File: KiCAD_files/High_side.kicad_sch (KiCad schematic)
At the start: 26 parts, among them U601 AMC1311DWV

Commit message: WIP
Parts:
- removed TP? (x4): TestPoint, Footprints:TestPoint_THTPad_D1.5mm_Drill0.7mm, symbol Connector:TestPoint
- added TP202 (x4): TestPoint, Footprints:TestPoint_THTPad_D1.5mm_Drill0.7mm, symbol Connector:TestPoint
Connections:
- net DGND: now also TP202.1, TP202.1
- net I_{IHigh_sense_DGND}: now also TP202.1
- net V_{IHighOutFused_PGND}: now also U?.1 (IP+), U?.2 (IP+); no longer U?.3 (IP-), U?.4 (IP-)
- net V_{IHigh_PGND}: now also U?.3 (IP-), U?.4 (IP-); no longer U?.1 (IP+), U?.2 (IP+)
- net V_{IHigh_sense_DGND}: now also TP202.1
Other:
- moved on the sheet: U?

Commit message: big clean in libraries (imported components in symbol), PCB WIP
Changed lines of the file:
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@@
     )
     (property "Value" "OPA316" (at 128.27 190.5 0)
-      (effects (font (size 1.27 1.27)) (justify left))
+      (effects (font (size 1.27 1.27)) (justify left) hide)
     )
     (property "Footprint" "Package_TO_SOT_SMD:SOT-353_SC-70-5_Handsoldering" (at 130.81 199.39 0)
@@
     )
     (property "manf#" "OPA316IDCKT" (at 125.73 194.31 0)
-      (effects (font (size 1.27 1.27)) hide)
+      (effects (font (size 1.27 1.27)))
     )
     (pin "1")

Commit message: Ready for design review
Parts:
- removed C? (x2): 100nF, Footprints:C_0805_2012Metric, symbol Device:C_Small
- added C? (x2): 100nF, Capacitor_SMD:C_1206_3216Metric, symbol Device:C_Small
- C?: footprint Footprints:C_0805_2012Metric -> Capacitor_SMD:C_1206_3216Metric; Functional Block (none) -> Measurement; Metal content (none) -> BaTiO3; Package 0805 -> 1206; Subfunction (none) -> VIHigh measure; manf# C0805C104K5RACTU -> C1206C104K5RAC7867
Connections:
- net +5V_DGND: now also C?.2
- net +5V_PGND: now also C?.2
- net DGND: now also C?.1
- net PGND: now also C?.1
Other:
- moved on the sheet: C?
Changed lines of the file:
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@@
     (stroke (width 0.35) (type default))
   )
-  (wire (pts (xy 88.9 170.18) (xy 88.9 171.45))
+  (wire (pts (xy 88.9 170.18) (xy 88.9 172.72))
     (stroke (width 0) (type default))
   )
@@
     (stroke (width 0) (type default))
   )
-  (wire (pts (xy 88.9 176.53) (xy 88.9 180.34))
+  (wire (pts (xy 88.9 177.8) (xy 88.9 180.34))
     (stroke (width 0) (type default))
   )
@@
     )
   )
-  (symbol (lib_id "Device:C_Small") (at 88.9 173.99 0) (mirror x) (unit 1)
-    (in_bom yes) (on_board yes) (dnp no)
-    (property "Reference" "C?" (at 91.44 172.72 0)
-      (effects (font (size 1.27 1.27)) (justify left))
-    )
-    (property "Value" "100nF" (at 90.17 176.53 0)
-      (effects (font (size 1.27 1.27)) (justify left))
-    )
-    (property "Footprint" "Footprints:C_0805_2012Metric" (at 88.9 173.99 0)
-      (effects (font (size 1.27 1.27)) hide)
-    )
-    (property "Datasheet" "~" (at 88.9 173.99 0)
-      (effects (font (size 1.27 1.27)) hide)
-    )
-    (property "manf#" "C0805C104K5RACTU" (at 88.9 173.99 0)
-      (effects (font (size 1.27 1.27)) hide)
-    )
-    (property "DNP" "x" (at 88.9 173.99 0)
-      (effects (font (size 1.27 1.27)) hide)
-    )
-    (property "Voltage" "50V" (at 87.63 170.18 90)
-      (effects (font (size 1.27 1.27)) hide)
-    )
-    (property "Package" "0805" (at 91.44 170.18 90)
+  (symbol (lib_id "Device:C_Small") (at 88.9 175.26 0) (mirror x) (unit 1)
+    (in_bom yes) (on_board yes) (dnp no)
+    (property "Reference" "C?" (at 91.44 173.99 0)
+      (effects (font (size 1.27 1.27)) (justify left))
+    )
+    (property "Value" "100nF" (at 91.44 176.53 0)
+      (effects (font (size 1.27 1.27)) (justify left))
+    )
+    (property "Footprint" "Capacitor_SMD:C_1206_3216Metric" (at 88.9 175.26 0)
+      (effects (font (size 1.27 1.27)) hide)
+    )
+    (property "Datasheet" "~" (at 88.9 175.26 0)
+      (effects (font (size 1.27 1.27)) hide)
+    )
+    (property "manf#" "C1206C104K5RAC7867" (at 88.9 175.26 0)
+      (effects (font (size 1.27 1.27)) hide)
+    )
+    (property "DNP" "x" (at 88.9 175.26 0)
+      (effects (font (size 1.27 1.27)) hide)
+    )
+    (property "Voltage" "50V" (at 87.63 171.45 90)
+      (effects (font (size 1.27 1.27)) hide)
+    )
+    (property "Package" "1206" (at 93.98 179.07 0)
+      (effects (font (size 1.27 1.27)))
+    )
+    (property "Functional Block" "Measurement" (at 88.9 175.26 0)
+      (effects (font (size 1.27 1.27)) hide)
+    )
+    (property "Metal content" "BaTiO3" (at 88.9 175.26 0)
+      (effects (font (size 1.27 1.27)) hide)
+    )
+    (property "Subfunction" "VIHigh measure" (at 88.9 175.26 0)
       (effects (font (size 1.27 1.27)) hide)
     )
@@
         (path "/8d0c1d66-35ef-4a53-a28f-436a11b54f42/e045b567-5361-4b1d-a1af-a53fa67ecaba"
           (reference "R604") (unit 1)
-        )
-      )
-    )
-  )
-  (symbol (lib_id "Device:C_Small") (at 113.03 67.31 0) (mirror x) (unit 1)
-    (in_bom yes) (on_board yes) (dnp no)
-    (property "Reference" "C?" (at 115.57 66.04 0)
-      (effects (font (size 1.27 1.27)) (justify left))
-    )
-    (property "Value" "100nF" (at 114.3 69.85 0)
-      (effects (font (size 1.27 1.27)) (justify left))
-    )
-    (property "Footprint" "Footprints:C_0805_2012Metric" (at 113.03 67.31 0)
-      (effects (font (size 1.27 1.27)) hide)
-    )
-    (property "Datasheet" "~" (at 113.03 67.31 0)
-      (effects (font (size 1.27 1.27)) hide)
-    )
-    (property "manf#" "C0805C104K5RACTU" (at 113.03 67.31 0)
-      (effects (font (size 1.27 1.27)) hide)
-    )
-    (property "DNP" "x" (at 113.03 67.31 0)
-      (effects (font (size 1.27 1.27)) hide)
-    )
-    (property "Voltage" "50V" (at 111.76 63.5 90)
-      (effects (font (size 1.27 1.27)) hide)
-    )
-    (property "Package" "0805" (at 115.57 63.5 90)
-      (effects (font (size 1.27 1.27)) hide)
-    )
-    (pin "1")
-    (pin "2")
-    (instances
-      (project "InverterLeg"
-        (path "/22b63e0d-f11c-46a0-b2d0-b08207a579ff"
-          (reference "C?") (unit 1)
-        )
-      )
-      (project "Power"
-        (path "/8d0c1d66-35ef-4a53-a28f-436a11b54f42/122c01f4-f23e-4db0-9503-7261d96dc78b"
-          (reference "C?") (unit 1)
-        )
-        (path "/8d0c1d66-35ef-4a53-a28f-436a11b54f42/e045b567-5361-4b1d-a1af-a53fa67ecaba"
-          (reference "C604") (unit 1)
         )
       )
@@
     )
   )
-  (symbol (lib_id "Device:C_Small") (at 50.8 175.26 0) (mirror y) (unit 1)
-    (in_bom yes) (on_board yes) (dnp no)
-    (property "Reference" "C?" (at 48.26 176.53 0)
-      (effects (font (size 1.27 1.27)) (justify left))
-    )
-    (property "Value" "100nF" (at 49.53 172.72 0)
-      (effects (font (size 1.27 1.27)) (justify left))
-    )
-    (property "Footprint" "Footprints:C_0805_2012Metric" (at 50.8 175.26 0)
-      (effects (font (size 1.27 1.27)) hide)
-    )
-    (property "Datasheet" "~" (at 50.8 175.26 0)
-      (effects (font (size 1.27 1.27)) hide)
-    )
-    (property "manf#" "C0805C104K5RACTU" (at 50.8 175.26 0)
-      (effects (font (size 1.27 1.27)) hide)
-    )
-    (property "DNP" "x" (at 50.8 175.26 0)
-      (effects (font (size 1.27 1.27)) hide)
-    )
-    (property "Voltage" "50V" (at 52.07 179.07 90)
-      (effects (font (size 1.27 1.27)) hide)
-    )
-    (property "Package" "0805" (at 48.26 179.07 90)
+  (symbol (lib_id "Device:C_Small") (at 113.03 67.31 0) (mirror x) (unit 1)
+    (in_bom yes) (on_board yes) (dnp no)
+    (property "Reference" "C?" (at 115.57 66.04 0)
+      (effects (font (size 1.27 1.27)) (justify left))
+    )
+    (property "Value" "100nF" (at 115.57 68.58 0)
+      (effects (font (size 1.27 1.27)) (justify left))
+    )
+    (property "Footprint" "Capacitor_SMD:C_1206_3216Metric" (at 113.03 67.31 0)
+      (effects (font (size 1.27 1.27)) hide)
+    )
+    (property "Datasheet" "~" (at 113.03 67.31 0)
+      (effects (font (size 1.27 1.27)) hide)
+    )
+    (property "manf#" "C1206C104K5RAC7867" (at 113.03 67.31 0)
+      (effects (font (size 1.27 1.27)) hide)
+    )
+    (property "DNP" "x" (at 113.03 67.31 0)
+      (effects (font (size 1.27 1.27)) hide)
+    )
+    (property "Voltage" "50V" (at 111.76 63.5 90)
+      (effects (font (size 1.27 1.27)) hide)
+    )
+    (property "Package" "1206" (at 118.11 71.12 0)
+      (effects (font (size 1.27 1.27)))
+    )
+    (property "Functional Block" "Measurement" (at 113.03 67.31 0)
+      (effects (font (size 1.27 1.27)) hide)
+    )
+    (property "Metal content" "BaTiO3" (at 113.03 67.31 0)
+      (effects (font (size 1.27 1.27)) hide)
+    )
+    (property "Subfunction" "VIHigh measure" (at 113.03 67.31 0)
       (effects (font (size 1.27 1.27)) hide)
     )
@@
         )
         (path "/8d0c1d66-35ef-4a53-a28f-436a11b54f42/e045b567-5361-4b1d-a1af-a53fa67ecaba"
-          (reference "C601") (unit 1)
+          (reference "C604") (unit 1)
         )
       )
@@
         )
       )
+    )
+  )
+  (symbol (lib_id "Device:C_Small") (at 50.8 175.26 180) (unit 1)
+    (in_bom yes) (on_board yes) (dnp no)
+    (property "Reference" "C?" (at 48.26 173.99 0)
+      (effects (font (size 1.27 1.27)) (justify left))
+    )
+    (property "Value" "100nF" (at 48.26 176.53 0)
+      (effects (font (size 1.27 1.27)) (justify left))
+    )
+    (property "Footprint" "Capacitor_SMD:C_1206_3216Metric" (at 50.8 175.26 0)
+      (effects (font (size 1.27 1.27)) hide)
+    )
+    (property "Datasheet" "~" (at 50.8 175.26 0)
+      (effects (font (size 1.27 1.27)) hide)
+    )
+    (property "manf#" "C1206C104K5RAC7867" (at 50.8 175.26 0)
+      (effects (font (size 1.27 1.27)) hide)
+    )
+    (property "DNP" "x" (at 50.8 175.26 0)
+      (effects (font (size 1.27 1.27)) hide)
+    )
+    (property "Voltage" "50V" (at 52.07 171.45 90)
+      (effects (font (size 1.27 1.27)) hide)
+    )
+    (property "Package" "1206" (at 45.72 179.07 0)
+      (effects (font (size 1.27 1.27)))
+    )
+    (property "Functional Block" "Measurement" (at 50.8 175.26 0)
+      (effects (font (size 1.27 1.27)) hide)
+    )
+    (property "Metal content" "BaTiO3" (at 50.8 175.26 0)
+      (effects (font (size 1.27 1.27)) hide)
+    )
+    (property "Subfunction" "VIHigh measure" (at 50.8 175.26 0)
+      (effects (font (size 1.27 1.27)) hide)
+    )
+    (pin "1")
+    (pin "2")
+    (instances
+      (project "InverterLeg"
+        (path "/22b63e0d-f11c-46a0-b2d0-b08207a579ff"
+          (reference "C?") (unit 1)
+        )
+      )
+      (project "Power"
+        (path "/8d0c1d66-35ef-4a53-a28f-436a11b54f42/122c01f4-f23e-4db0-9503-7261d96dc78b"
+          (reference "C?") (unit 1)
+        )
+        (path "/8d0c1d66-35ef-4a53-a28f-436a11b54f42/e045b567-5361-4b1d-a1af-a53fa67ecaba"
+          (reference "C601") (unit 1)
+        )
+      )

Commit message: dev
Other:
- note added: "ACS723 is pin to pin compatible with ACS12. If ACS723 is used, do not place filter capacitor on pin 6, tie pin 6 to ground, which forces bandwidth to 80kHz (tie it to VCC for 20kHz bandwidth)."
- note added: "PIN 6 (Filter) is designed to connect a capacitor to ground to form low pass RC filter with an internal capacitor of 1.7kOhm According to formula theoretical cutoff frequency is calculted like so : fc = 1/(2*pi*R*C) Here we have some examples of cutoff frequency for different values of capacitor ___________________ | C (nF) | fc (kHz) |------------ | 1 | 93.6 |------------ | 10 | 9.36 |----------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"
- moved on the sheet: C?, R?, TP202, U601, U?

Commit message: ready for design review
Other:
- note added: "DIGITAL AREA"
- note removed: "Digital AREA"

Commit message: wip
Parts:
- removed U?: +-20A Hall, Package_SO:SOIC-8_3.9x4.9mm_P1.27mm, symbol Symbols:ACS712ELCTR-20A-T
- added R?: 0R, Footprints:R_0805_2012Metric, symbol Device:R_Small
- added U602: ACS723LLCTR-20AB-T, Package_SO:SOIC-8_3.9x4.9mm_P1.27mm, symbol Symbols:ACS723LLCTR-20AB-T
- C?: DNP x -> DNP
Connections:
- net +5V_DGND: now also R?.1, U602.8 (VCC)
- net DGND: now also U602.5 (GND)
- net I_{IHighHall_DGND}: now also U602.7 (VIOUT)
- net V_{IHighOutFused_PGND}: now also U602.1 (IP+), U602.2 (IP+)
- net V_{IHigh_PGND}: now also U602.3 (IP-), U602.4 (IP-)
- net at C?.2: now also R?.2, U602.6 (BW_SEL)
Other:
- note added: "ACS712 is pin to pin compatible with ACS723. If ACS712 is used, untie pin 6 and place filter capacitor on pin 6, according to wanted BW."
- note added: "ACS723 pin 6 BW_SELECT : - tie to ground for 80kHz BW. - tie to VCC for 20kHz bandwidth."
- note added: "PIN 6 (Filter) of ACS712 is designed to connect a capacitor to ground to form low pass RC filter with an internal capacitor of 1.7kOhm According to formula theoretical cutoff frequency is calculted like so : fc = 1/(2*pi*R*C) Here we have some examples of cutoff frequency for different values of capacitor _________________ C (nF) | fc (kHz) ------------ 1 | 93.6 ------------ 10 | 9.36 -----------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"
- note removed: "ACS723 is pin to pin compatible with ACS12. If ACS723 is used, do not place filter capacitor on pin 6, tie pin 6 to ground, which forces bandwidth to 80kHz (tie it to VCC for 20kHz bandwidth)."
- note removed: "PIN 6 (Filter) is designed to connect a capacitor to ground to form low pass RC filter with an internal capacitor of 1.7kOhm According to formula theoretical cutoff frequency is calculted like so : fc = 1/(2*pi*R*C) Here we have some examples of cutoff frequency for different values of capacitor ___________________ | C (nF) | fc (kHz) |------------ | 1 | 93.6 |------------ | 10 | 9.36 |----------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"
- moved on the sheet: C?, R?

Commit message: wip
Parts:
- U? (x2): value OPA316 -> OPA316IDCKT
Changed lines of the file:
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@@
     (fill (type none))
   )
-  (text "VHIGH measure conditionning\n\n" (at 95.25 160.02 0)
-    (effects (font (face "Arial") (size 2.4892 2.4892) (thickness 0.4978) bold) (justify left bottom))
+  (text "VHIGH measure conditionning\n\n" (at 77.47 158.75 0)
+    (effects (font (face "Arial") (size 2.54 2.54) (thickness 0.4978) bold) (justify left bottom))
   )
   (text "ACS712 is pin to pin compatible\nwith ACS723. If ACS712 is used,\nuntie pin 6 and place\nfilter capacitor on pin 6,\naccording to wanted BW.\n"
@@
     (effects (font (size 1.27 1.27)) (justify left bottom))
   )
-  (text "IHigh and VHigh sense\n" (at 123.19 30.48 0)
-    (effects (font (face "Arial") (size 2.4892 2.4892) (thickness 0.4978) bold) (justify right bottom))
+  (text "IHigh and VHigh sense\n" (at 125.73 29.21 0)
+    (effects (font (face "Arial") (size 2.54 2.54) (thickness 0.4978) bold) (justify right bottom))
   )
   (text "VI_High_op has a 2,048V \namplitude without offset" (at 176.53 167.64 0)
@@
     (effects (font (face "Arial") (size 1.27 1.27)) (justify left bottom))
   )
-  (text "IHIGH measure conditionning\n\n" (at 200.66 160.02 0)
-    (effects (font (face "Arial") (size 2.4892 2.4892) (thickness 0.4978) bold) (justify left bottom))
+  (text "IHIGH measure conditionning\n\n" (at 198.12 158.75 0)
+    (effects (font (face "Arial") (size 2.54 2.54) (thickness 0.4978) bold) (justify left bottom))
   )
   (text "RG" (at 199.39 182.88 0)
@@
   )
   (text "DIGITAL AREA\n" (at 62.23 156.21 0)
-    (effects (font (face "Arial") (size 1.27 1.27)) (justify left bottom))
-  )
-  (text "DIGITAL AREA\n" (at 171.45 156.21 0)
     (effects (font (face "Arial") (size 1.27 1.27)) (justify left bottom))
   )
@@
       (effects (font (size 1.27 1.27)) (justify left))
     )
-    (property "Value" "OPA316" (at 224.79 179.07 0)
+    (property "Value" "OPA316IDCKT" (at 224.79 179.07 0)
       (effects (font (size 1.27 1.27)) (justify left) hide)
     )
@@
       (effects (font (size 1.27 1.27)) (justify left))
     )
-    (property "Value" "OPA316" (at 119.38 190.5 0)
+    (property "Value" "OPA316IDCKT" (at 119.38 190.5 0)
       (effects (font (size 1.27 1.27)) (justify left) hide)
     )
@@
       (effects (font (size 1.27 1.27)) hide)
     )
-    (property "Datasheet" "http://www.ti.com/lit/ds/symlink/tlv6001.pdf" (at 116.84 201.93 0)
+    (property "Datasheet" "https://www.ti.com/lit/ds/symlink/opa316.pdf?ts=1683791438609&ref_url=https%253A%252F%252Fwww.google.com%252F" (at 116.84 201.93 0)
       (effects (font (size 1.27 1.27)) hide)
     )
@@
       (effects (font (size 1.27 1.27)) hide)
     )
-    (property "Datasheet" "file:///C:/Users/twalter/Downloads/ACS723-Datasheet.pdf" (at 113.03 68.58 0)
-      (effects (font (size 1.27 1.27)) hide)
-    )
+    (property "Datasheet" "${KIPRJMOD}/Datasheet/1.pdf" (at 113.03 68.58 0)
+      (effects (font (size 1.27 1.27)) hide)
+    )

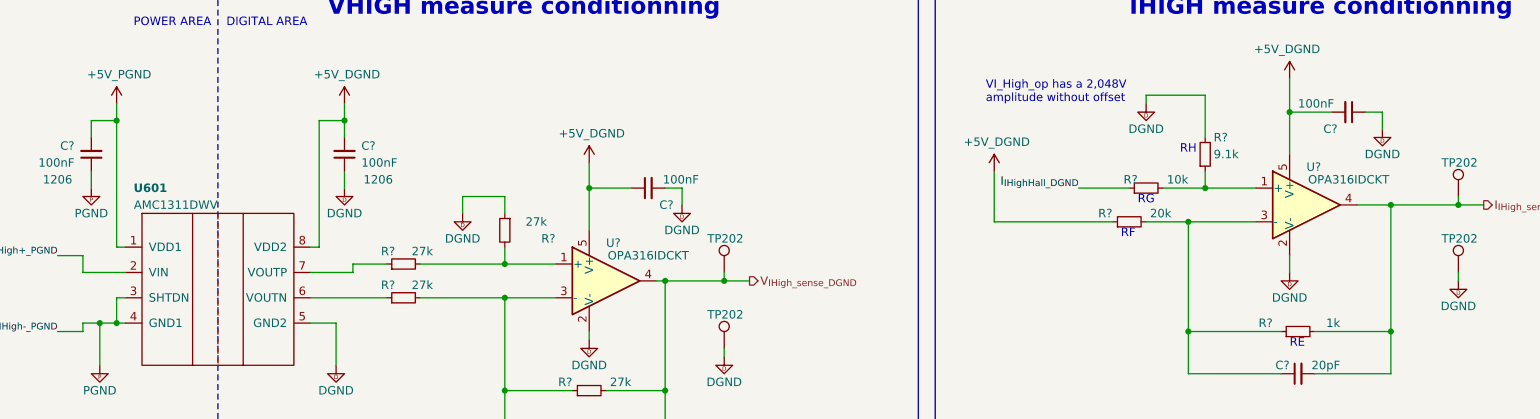
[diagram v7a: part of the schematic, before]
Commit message: moved datahsset folder into kicad files folder to use the KIPRJMOD venv that points to KICAD_files folder. Component datasheet filed redirects now to local file
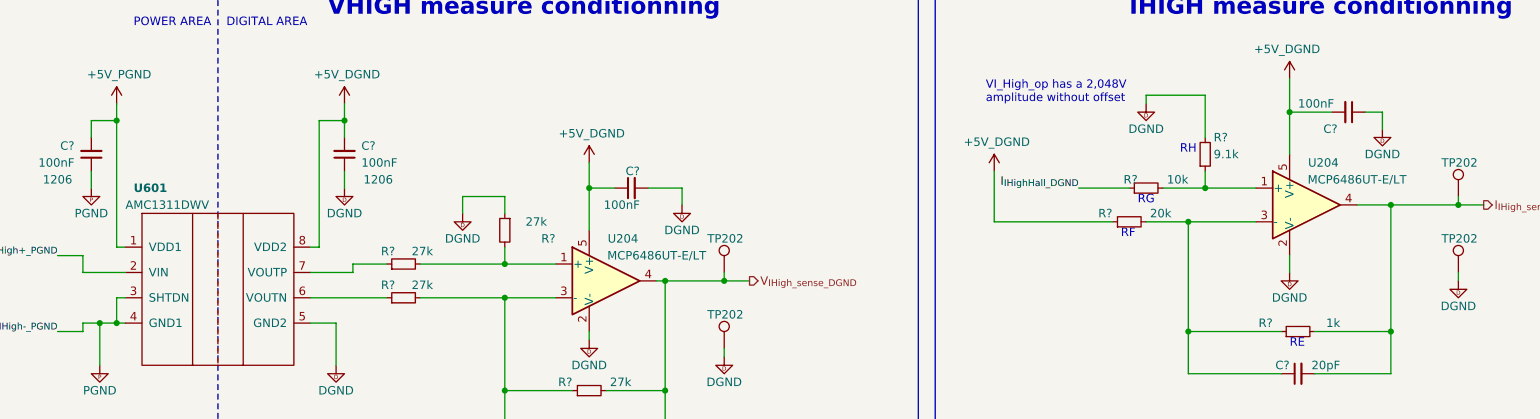
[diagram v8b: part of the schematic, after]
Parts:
- removed U? (x2): OPA316IDCKT, Package_TO_SOT_SMD:SOT-353_SC-70-5_Handsoldering, symbol Amplifier_Operational:TLV6001DCK
- added U204 (x2): MCP6486UT-E/LT, Package_TO_SOT_SMD:SOT-353_SC-70-5_Handsoldering, symbol Symbols:MCP6486UT-E/LT
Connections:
- net +5V_DGND: now also U204.5 (V+), U204.5 (V+)
- net DGND: now also U204.2 (V-), U204.2 (V-)
- net I_{IHigh_sense_DGND}: now also U204.4
- net V_{IHigh_sense_DGND}: now also U204.4
- net at C?.1, R?.1, R?.2: now also U204.3 (-) (x2)
- net at R?.1, R?.2: now also U204.1 (+)
- net at R?.2, R?.2: now also U204.1 (+)
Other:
- moved on the sheet: C?
